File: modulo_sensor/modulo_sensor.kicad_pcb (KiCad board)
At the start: 2 copper layers, 90 x 27 mm, 33 parts, among them J1 Conn_01x08_Pin, U1 74HC14DR2G

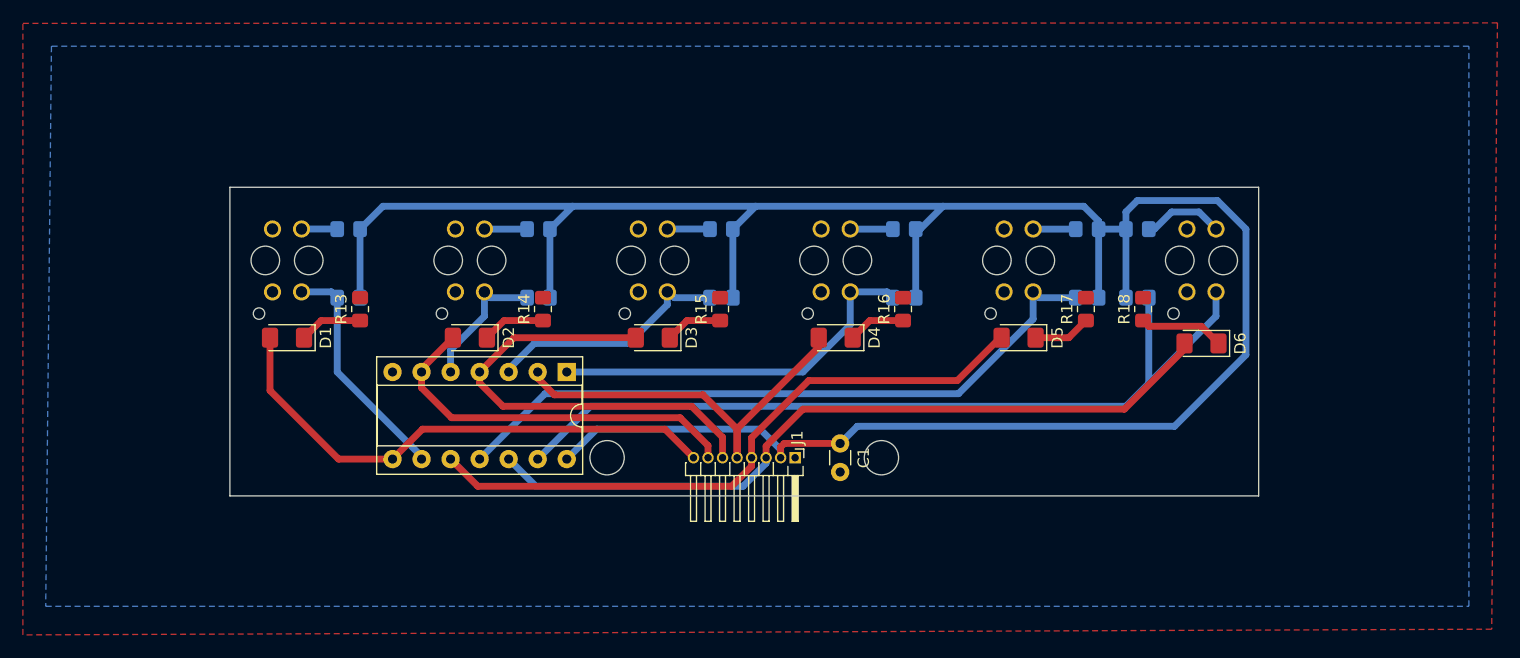
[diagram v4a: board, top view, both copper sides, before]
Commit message: refactor: Cambio ancho de pistas en el modulo sensor a 0,7mm
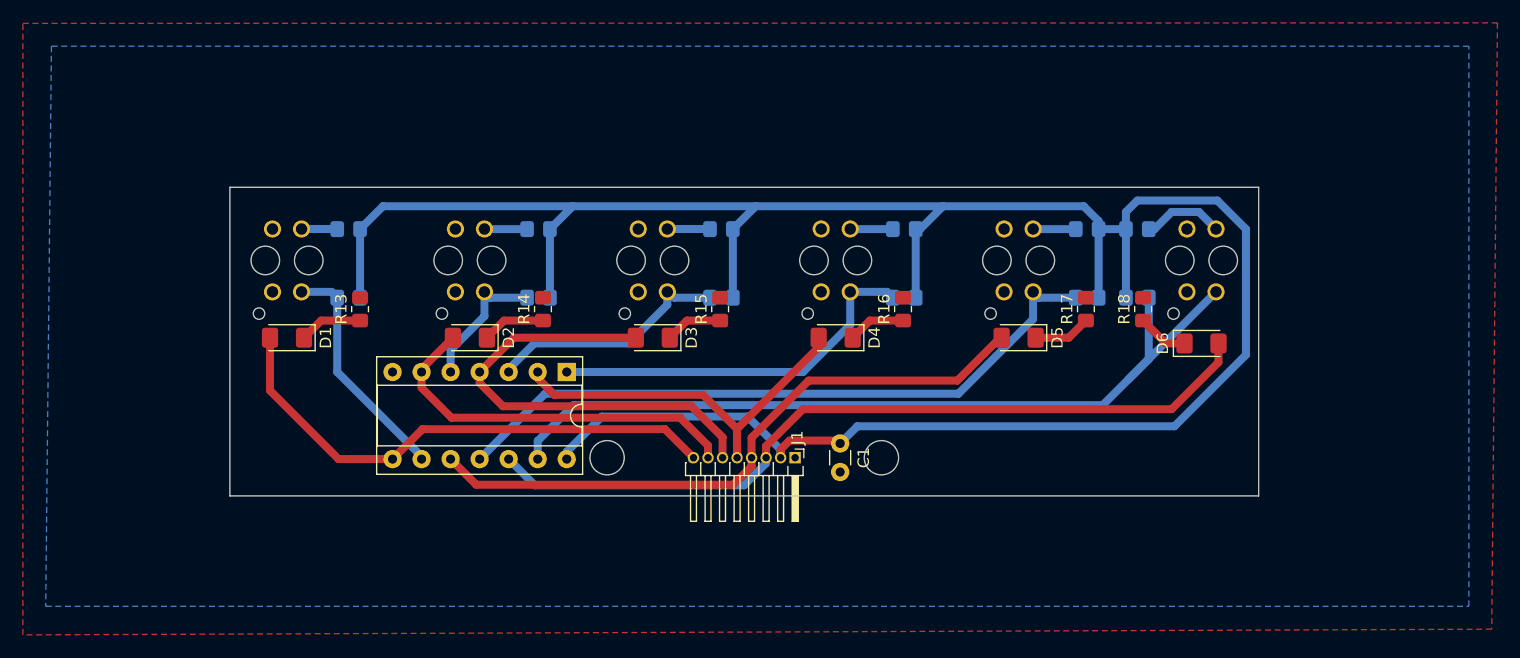
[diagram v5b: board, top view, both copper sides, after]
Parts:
- turned D6 to 0 degrees
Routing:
- net /Led_Sensor6: track 66.5 -> 70.1 mm
- net Net-(D6-K): track 7.43 -> 4.45 mm
- net vcc: track 204.6 -> 206.0 mm

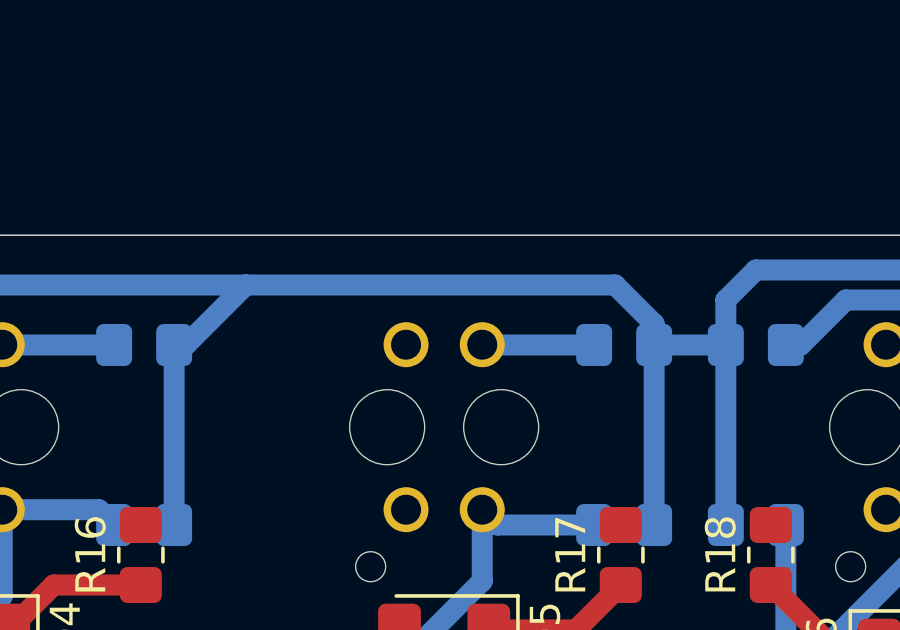
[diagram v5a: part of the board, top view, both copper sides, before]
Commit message: chore: Agrego aclaración para el led D6 espejado
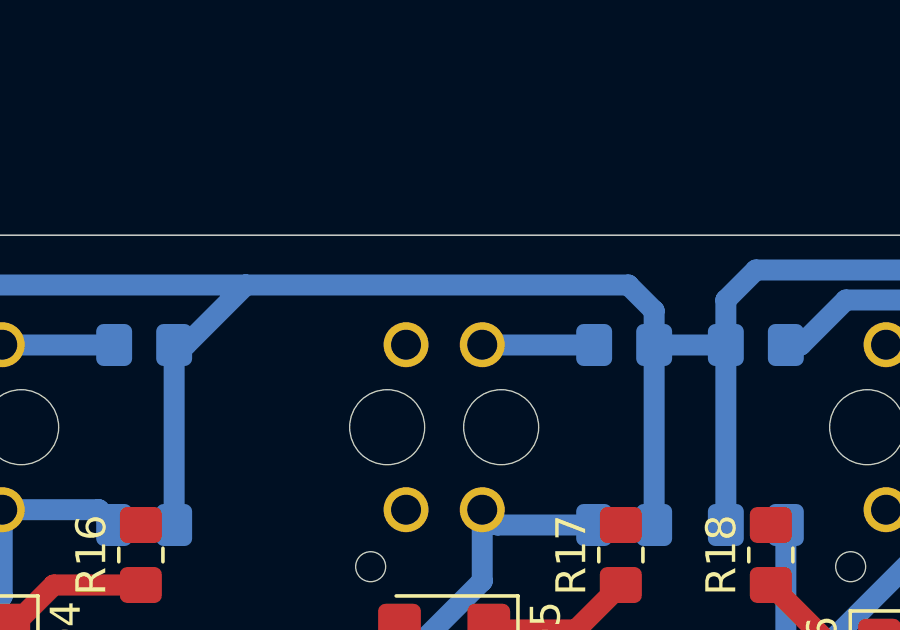
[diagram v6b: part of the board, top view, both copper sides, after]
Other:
- board text added: "LED D6 está al révés"
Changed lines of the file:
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@@
 		(layer "Edge.Cuts")
+	)
+	(gr_text "LED D6 está al révés"
+		(at 126.5 80.5 0)
+		(layer "Cmts.User")
+		(effects
+			(font
+				(size 1 1)
+				(thickness 0.15)
+			)
+			(justify left bottom)
+		)
 	)
 	(dimension
@@
 	)
 	(segment
-		(start 129.609983 59.3)
-		(end 128.309983 58)
-		(width 0.7)
-		(layer "B.Cu")
-		(net 1)
-	)
-	(segment
 		(start 129.609983 60)
 		(end 132 60)
@@
 	)
 	(segment
-		(start 128.309983 58)
-		(end 116 58)
-		(width 0.7)
-		(layer "B.Cu")
-		(net 1)
-	)
-	(segment
 		(start 132 58.5)
 		(end 132 60)
@@
 	)
 	(segment
+		(start 129.609983 60)
+		(end 129.609983 58.859983)
+		(width 0.7)
+		(layer "B.Cu")
+		(net 1)
+	)
+	(segment
 		(start 97.609983 60)
 		(end 97.609983 59.99099)
@@
 	)
 	(segment
+		(start 129.609983 58.859983)
+		(end 128.75 58)
+		(width 0.7)
+		(layer "B.Cu")
+		(net 1)
+	)
+	(segment
 		(start 133 57.5)
 		(end 132 58.5)
@@
 	)
 	(segment
+		(start 128.75 58)
+		(end 116 58)
+		(width 0.7)
+		(layer "B.Cu")
+		(net 1)
+	)
+	(segment
 		(start 113.609983 60)
 		(end 114 60)
@@
 		(width 0.7)
 		(layer "B.Cu")
-		(net 1)
-	)
-	(segment
-		(start 129.609983 60)
-		(end 129.609983 59.3)
-		(width 0.7)
-		(layer "B.Cu")
